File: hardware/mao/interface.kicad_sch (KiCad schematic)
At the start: 27 parts, among them J301 LCD, J302 TOUCH TOP, J303 TOUCH REAR, Q301 AO3400A, SW301 SKQGADE010, U301 DRV5012AEDMRR, U302 DRV5012AEDMRR

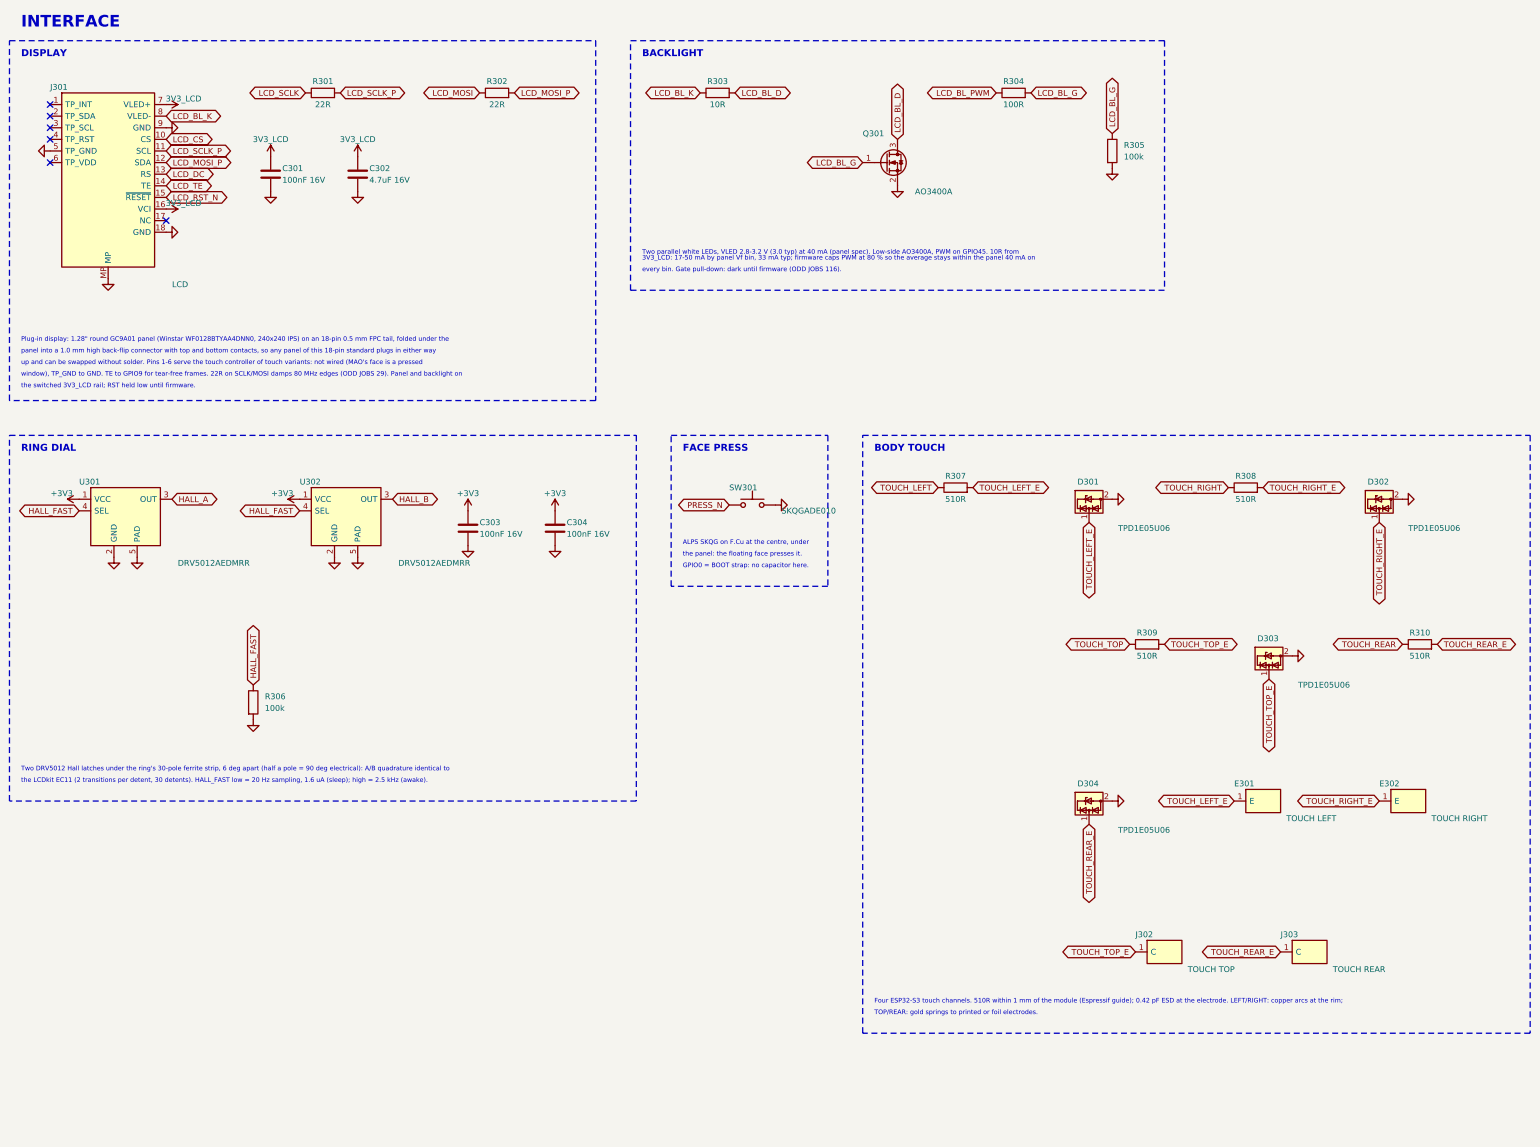
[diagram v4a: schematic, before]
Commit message: MAO A0 revision: stock Winstar panel through a tail slot, AW9364 backlight, routed 4-layer board
Hardware changes from the verification audits:
- display: stock Winstar WF0128BTYAA4DNN0 (70 mm tail) through a routed slot at 9 o'clock
  to J301 on B.Cu; panel pin k on pad 19-k
- backlight: VLED+ on VSYS into an AW9364 (U303) constant-current sink, 40 mA nominal;
  Q301/R303-R305 removed
- display rail: TPS22919 (SC70-6, 1.1 mm: fits under the panel) with its VIN cap; CT cap gone
- +3V3 at 3.18 V (FB 536k), UVLO filter cap, charger ISET 4.3k (207 mA), /CE from the
  expander with a pull-down, charger moved to F under the panel, SD_MODE series 2.2k
- IR_TX on GPIO38, EXP_RST_N on GPIO39 (MTCK reset pull-up lit the IR LEDs)
- IR receiver and ToF pulled inside the ring lip; M2 boss / screw-head keep-outs

Layout: re-placed and re-routed. DRC 0 violations, 0 unconnected; every plane one piece
(the grid router now undoes any L3 route or via that splits a plane); 192 through vias.
Silk: type scale, 6 x 6 S/N field with the JLC order-number placeholder, 4.6 mm back mark,
references kept off vias, and a few easter eggs (a sleeping cat under the face, boop,
meow, 9 lives, MADE FOR BAD IDEAS).

Checks: ERC 0, silk text 0 findings, enclosure check 0 findings (mech_check.py), all
simulations pass (S3 AW9364, S10 TPS22919, S13 207 mA). Docs: bring-up, factory test,
power budget, architecture, mechanical (tail path), pin map. Firmware: dev command
"mao power charge off|on", self-test pad floor for the 3.18 V rail; merge patch regenerated.

Co-Authored-By: Claude Opus 5.5 <noreply@anthropic.com>
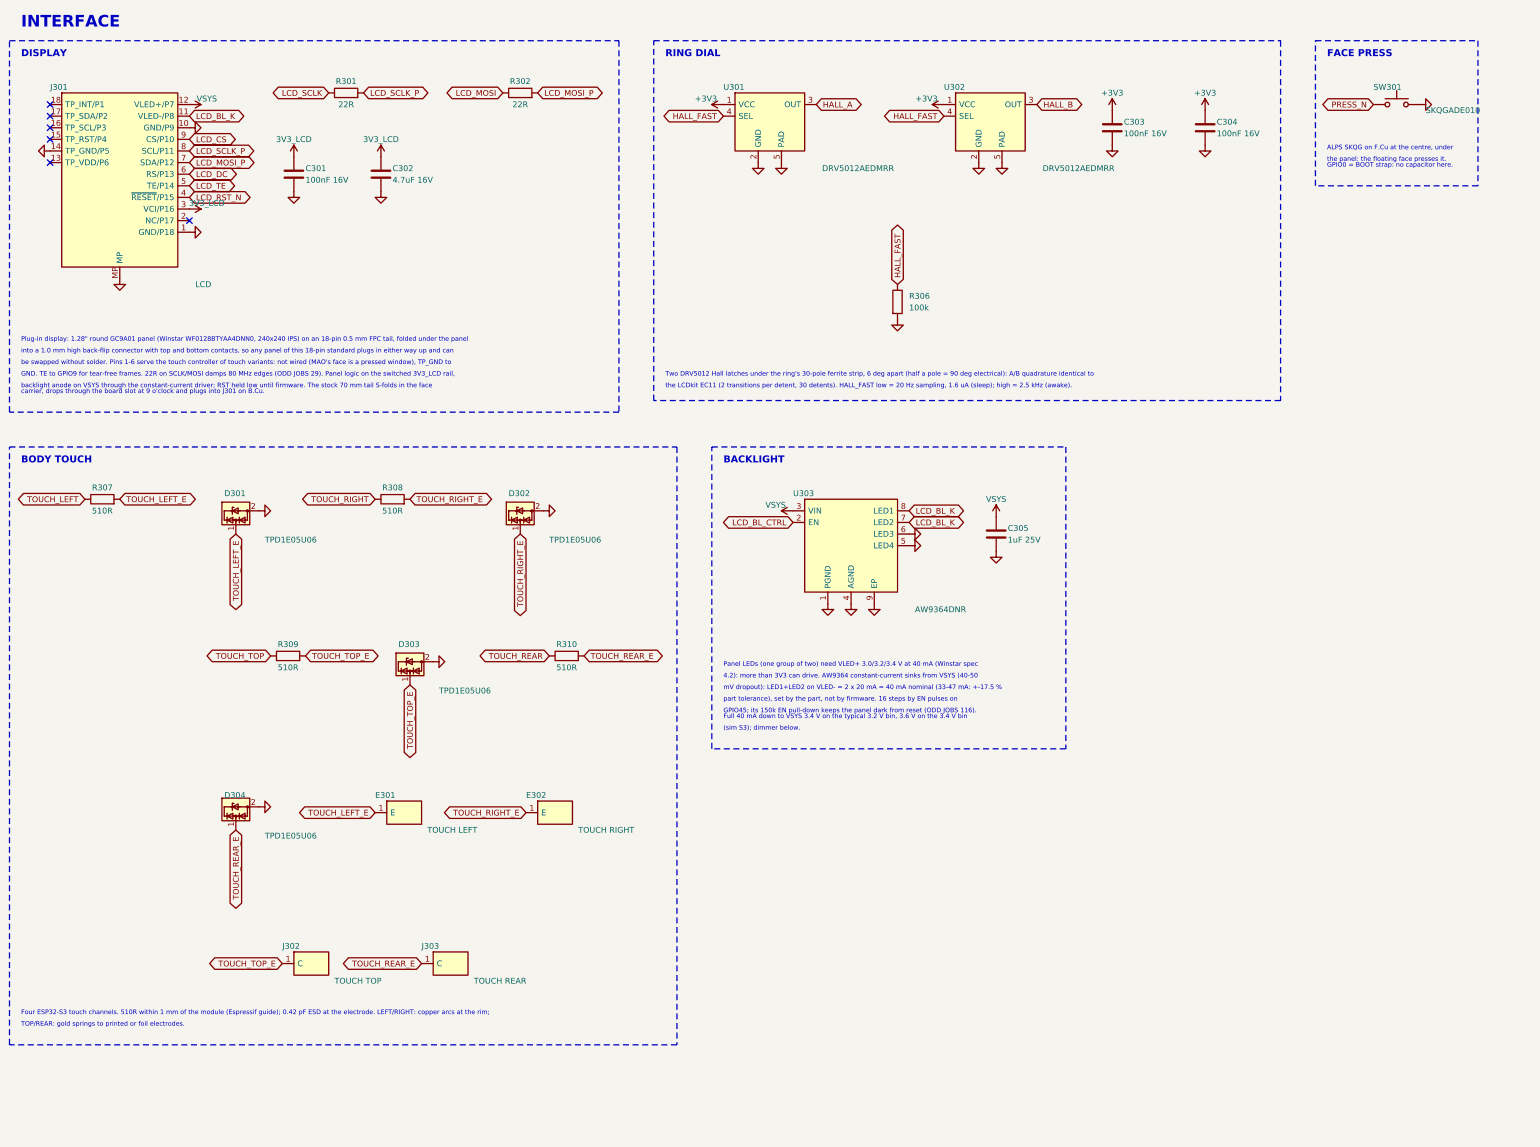
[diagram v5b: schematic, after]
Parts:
- removed Q301: AO3400A, Package_TO_SOT_SMD:SOT-23, symbol Transistor_FET:AO3400A
- removed R303: 10R, Resistor_SMD:R_0603_1608Metric, symbol Device:R
- removed R304: 100R, Resistor_SMD:R_0402_1005Metric, symbol Device:R
- removed R305: 100k, Resistor_SMD:R_0402_1005Metric, symbol Device:R
- added C305: 1uF 25V, Capacitor_SMD:C_0402_1005Metric, symbol Device:C
- added U303: AW9364DNR, Package_DFN_QFN:DFN-8-1EP_2x2mm_P0.5mm_EP0.6x1.2mm, symbol MAO:AW9364
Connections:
- net 3V3_LCD: now also J301.3 (VCI/P16); no longer J301.16 (VCI), J301.7 (VLED+)
- net GND: now also J301.1 (GND/P18), J301.10 (GND/P9), J301.14 (TP_GND/P5), C305.2, U303.1 (PGND), U303.4 (AGND), U303.5 (LED4), U303.6 (LED3), U303.9 (EP); no longer J301.18 (GND), J301.5 (TP_GND), J301.9 (GND)
- net LCD_BL_K: now also J301.11 (VLED-/P8), U303.7 (LED2), U303.8 (LED1); no longer J301.8 (VLED-)
- net LCD_CS: now also J301.9 (CS/P10); no longer J301.10 (CS)
- net LCD_DC: now also J301.6 (RS/P13); no longer J301.13 (RS)
- net LCD_MOSI_P: now also J301.7 (SDA/P12); no longer J301.12 (SDA)
- net LCD_RST_N: now also J301.4 (~{RESET}/P15); no longer J301.15 (~{RESET})
- net LCD_SCLK_P: now also J301.8 (SCL/P11); no longer J301.11 (SCL)
- net LCD_TE: now also J301.5 (TE/P14); no longer J301.14 (TE)
- new net LCD_BL_CTRL: U303.2 (EN)
- new net VSYS: C305.1, J301.12 (VLED+/P7), U303.3 (VIN)
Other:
- note added: "(sim S3); dimmer below."
- note added: "4.2): more than 3V3 can drive. AW9364 constant-current sinks from VSYS (40-50"
- note added: "Full 40 mA down to VSYS 3.4 V on the typical 3.2 V bin, 3.6 V on the 3.4 V bin"
- note added: "GND. TE to GPIO9 for tear-free frames. 22R on SCLK/MOSI damps 80 MHz edges (ODD JOBS 29). Panel logic on the switched 3V3_LCD rail,"
- note added: "GPIO45; its 150k EN pull-down keeps the panel dark from reset (ODD JOBS 116)."
- note added: "Panel LEDs (one group of two) need VLED+ 3.0/3.2/3.4 V at 40 mA (Winstar spec"
- note added: "Plug-in display: 1.28" round GC9A01 panel (Winstar WF0128BTYAA4DNN0, 240x240 IPS) on an 18-pin 0.5 mm FPC tail, folded under the panel"
- note added: "backlight anode on VSYS through the constant-current driver; RST held low until firmware. The stock 70 mm tail S-folds in the face"
- note added: "be swapped without solder. Pins 1-6 serve the touch controller of touch variants: not wired (MAO's face is a pressed window), TP_GND to"
- note added: "carrier, drops through the board slot at 9 o'clock and plugs into J301 on B.Cu."
- note added: "into a 1.0 mm high back-flip connector with top and bottom contacts, so any panel of this 18-pin standard plugs in either way up and can"
- note added: "mV dropout): LED1+LED2 on VLED- = 2 x 20 mA = 40 mA nominal (33-47 mA: +-17.5 %"
- note added: "part tolerance), set by the part, not by firmware. 16 steps by EN pulses on"
- note removed: "3V3_LCD: 17-50 mA by panel Vf bin, 33 mA typ; firmware caps PWM at 80 % so the average stays within the panel 40 mA on"
- note removed: "Plug-in display: 1.28" round GC9A01 panel (Winstar WF0128BTYAA4DNN0, 240x240 IPS) on an 18-pin 0.5 mm FPC tail, folded under the"
- note removed: "Two parallel white LEDs, VLED 2.8-3.2 V (3.0 typ) at 40 mA (panel spec). Low-side AO3400A, PWM on GPIO45. 10R from"
- note removed: "every bin. Gate pull-down: dark until firmware (ODD JOBS 116)."
- note removed: "panel into a 1.0 mm high back-flip connector with top and bottom contacts, so any panel of this 18-pin standard plugs in either way"
- note removed: "the switched 3V3_LCD rail; RST held low until firmware."
- note removed: "up and can be swapped without solder. Pins 1-6 serve the touch controller of touch variants: not wired (MAO's face is a pressed"
- note removed: "window), TP_GND to GND. TE to GPIO9 for tear-free frames. 22R on SCLK/MOSI damps 80 MHz edges (ODD JOBS 29). Panel and backlight on"
- moved on the sheet: C301, C302, C303, C304, D301, D302, D303, D304, E301, E302, J301, J302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

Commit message: MAO A0 schematic: one frame per block, wired local nets, no overprinted names
ODD JOBS audit 2, X8 (rules 187, 188):
- Parts added late (C111, R117, R507) join their block's frame instead of opening a duplicate frame
  with a copy of its note that ran over the neighbours.
- A two-pin part on a net that only joins it to one side pin of its block's IC is wired to that pin
  (the pin's label still names the net, so board, rules and procedures keep their names); feedback and
  UVLO-style dividers hang off their pin as a divider column. Columns step so no wire crosses a part.
- Adjacent pins on one rail share one rail symbol, joined by a wire; a sideways rail symbol keeps its
  name on its own row; turned passives, LEDs and diodes keep their reference and value off the body.
- Rail-source declarations sit in their own frame in the layout flow, not over the title block.
- Two stale notes corrected (C105 distance to VIN, R204 A0 voltage); board fields synced.

ERC 0, DRC 0 / 0 / parity 0.

Co-Authored-By: Claude Opus 5.5 <noreply@anthropic.com>
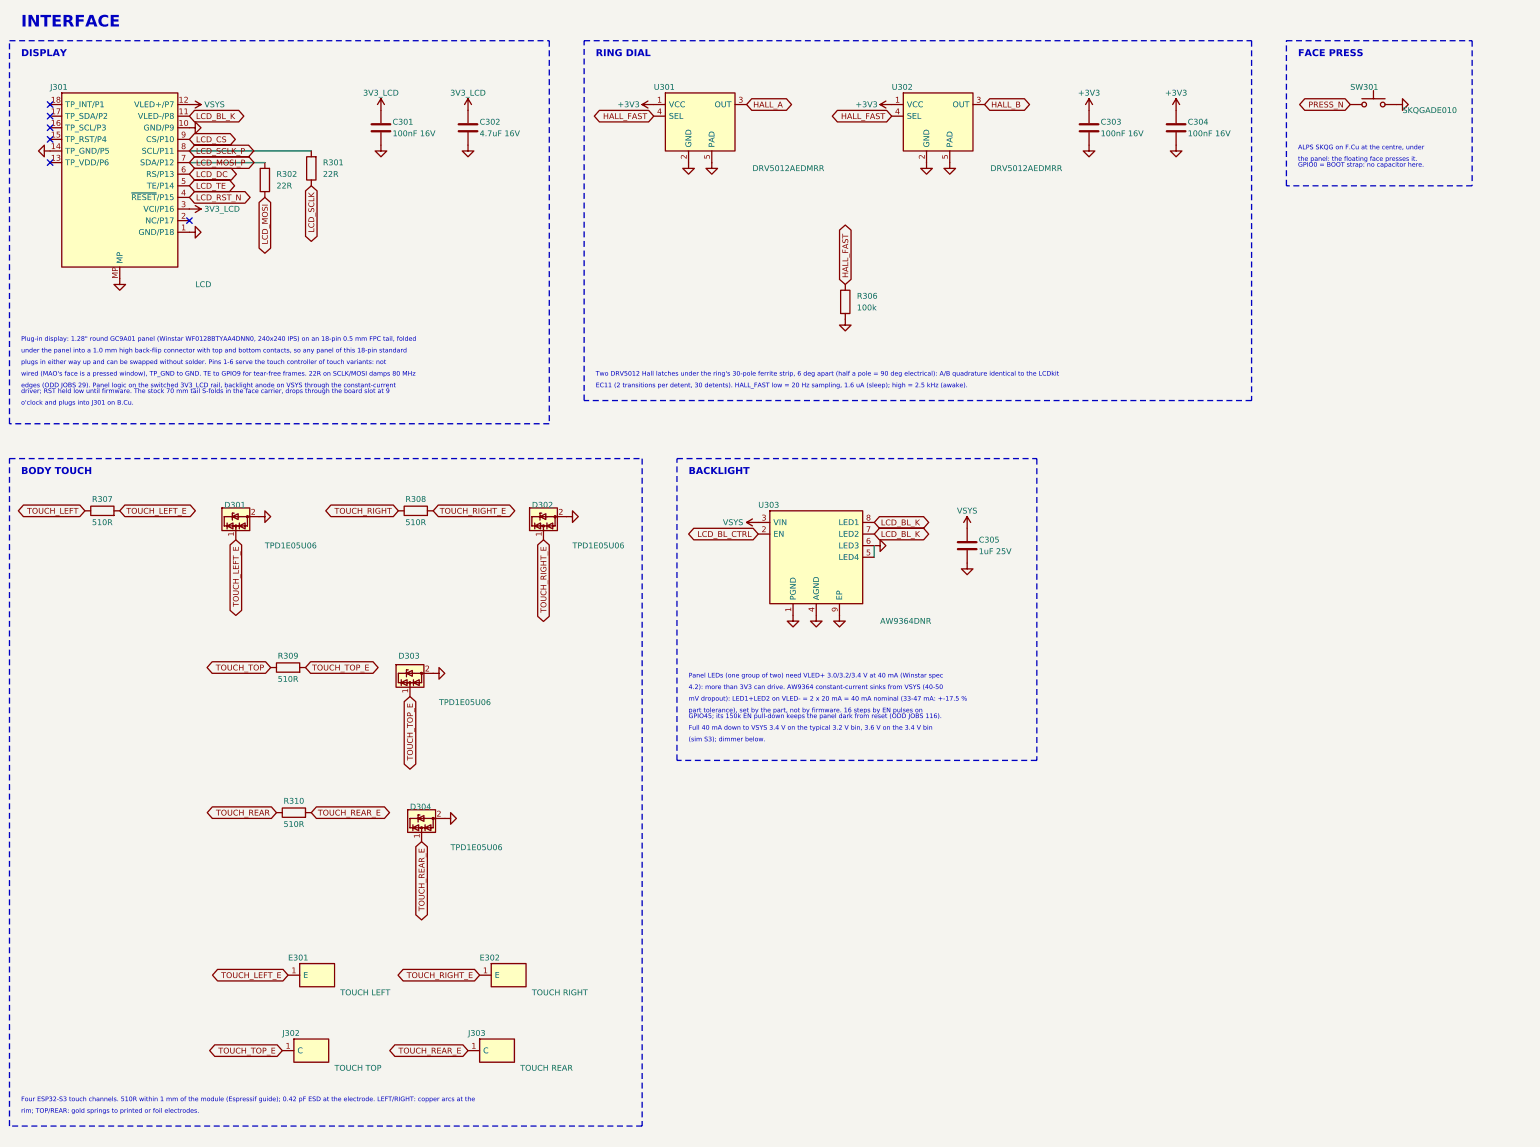
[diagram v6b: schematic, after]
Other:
- note added: "EC11 (2 transitions per detent, 30 detents). HALL_FAST low = 20 Hz sampling, 1.6 uA (sleep); high = 2.5 kHz (awake)."
- note added: "Four ESP32-S3 touch channels. 510R within 1 mm of the module (Espressif guide); 0.42 pF ESD at the electrode. LEFT/RIGHT: copper arcs at the"
- note added: "Plug-in display: 1.28" round GC9A01 panel (Winstar WF0128BTYAA4DNN0, 240x240 IPS) on an 18-pin 0.5 mm FPC tail, folded"
- note added: "Two DRV5012 Hall latches under the ring's 30-pole ferrite strip, 6 deg apart (half a pole = 90 deg electrical): A/B quadrature identical to the LCDkit"
- note added: "driver; RST held low until firmware. The stock 70 mm tail S-folds in the face carrier, drops through the board slot at 9"
- note added: "edges (ODD JOBS 29). Panel logic on the switched 3V3_LCD rail, backlight anode on VSYS through the constant-current"
- note added: "o'clock and plugs into J301 on B.Cu."
- note added: "plugs in either way up and can be swapped without solder. Pins 1-6 serve the touch controller of touch variants: not"
- note added: "rim; TOP/REAR: gold springs to printed or foil electrodes."
- note added: "under the panel into a 1.0 mm high back-flip connector with top and bottom contacts, so any panel of this 18-pin standard"
- note added: "wired (MAO's face is a pressed window), TP_GND to GND. TE to GPIO9 for tear-free frames. 22R on SCLK/MOSI damps 80 MHz"
- note removed: "Four ESP32-S3 touch channels. 510R within 1 mm of the module (Espressif guide); 0.42 pF ESD at the electrode. LEFT/RIGHT: copper arcs at the rim;"
- note removed: "GND. TE to GPIO9 for tear-free frames. 22R on SCLK/MOSI damps 80 MHz edges (ODD JOBS 29). Panel logic on the switched 3V3_LCD rail,"
- note removed: "Plug-in display: 1.28" round GC9A01 panel (Winstar WF0128BTYAA4DNN0, 240x240 IPS) on an 18-pin 0.5 mm FPC tail, folded under the panel"
- note removed: "TOP/REAR: gold springs to printed or foil electrodes."
- note removed: "Two DRV5012 Hall latches under the ring's 30-pole ferrite strip, 6 deg apart (half a pole = 90 deg electrical): A/B quadrature identical to"
- note removed: "backlight anode on VSYS through the constant-current driver; RST held low until firmware. The stock 70 mm tail S-folds in the face"
- note removed: "be swapped without solder. Pins 1-6 serve the touch controller of touch variants: not wired (MAO's face is a pressed window), TP_GND to"
- note removed: "carrier, drops through the board slot at 9 o'clock and plugs into J301 on B.Cu."
- note removed: "into a 1.0 mm high back-flip connector with top and bottom contacts, so any panel of this 18-pin standard plugs in either way up and can"
- note removed: "the LCDkit EC11 (2 transitions per detent, 30 detents). HALL_FAST low = 20 Hz sampling, 1.6 uA (sleep); high = 2.5 kHz (awake)."
- moved on the sheet: C301, C302, C303, C304, C305, D301, D302, D303, D304, E301, E302, J302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
